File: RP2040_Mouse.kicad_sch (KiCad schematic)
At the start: 35 parts, among them J1 DB9_Male, J2 Barrel_Jack_Switch, J3 USB_A, Q1 Q_NPN_BEC, SW1 SW_DPDT_x2, U1 LSF0108PWR, U2 RP2040, U3 AT25SF081B-SSHD-T, U4 AMS1117-3.3, Y1 12MHZ

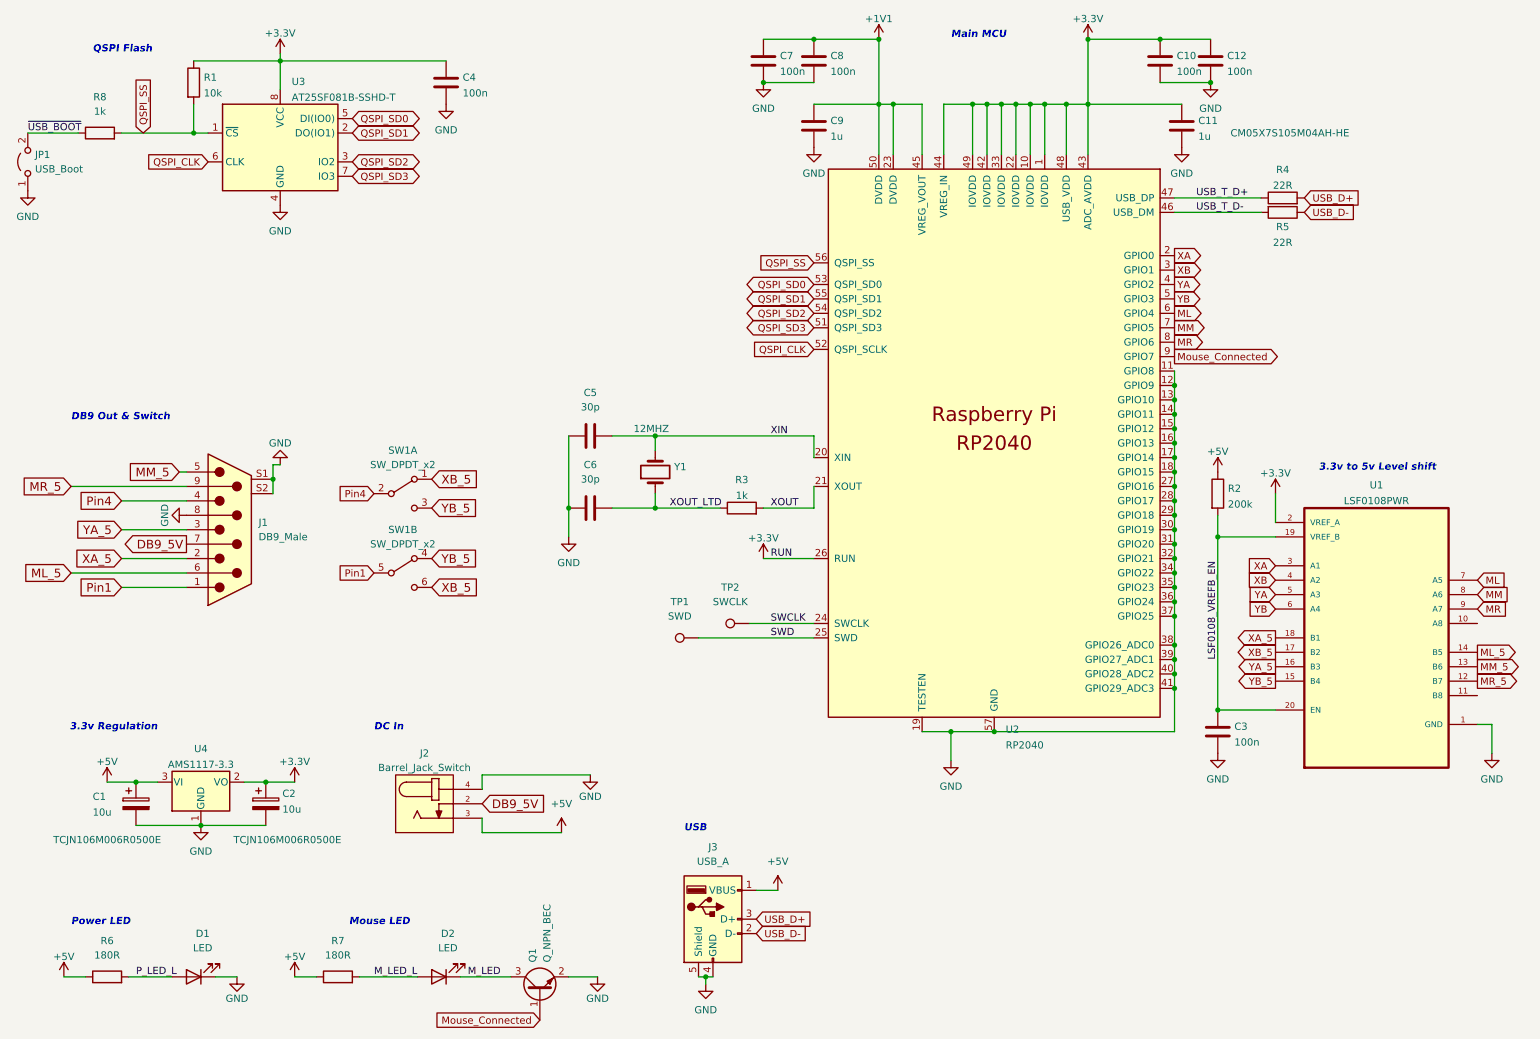
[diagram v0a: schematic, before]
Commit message: Added pullup resistors on mouse buttons, added breakout points for user software updates
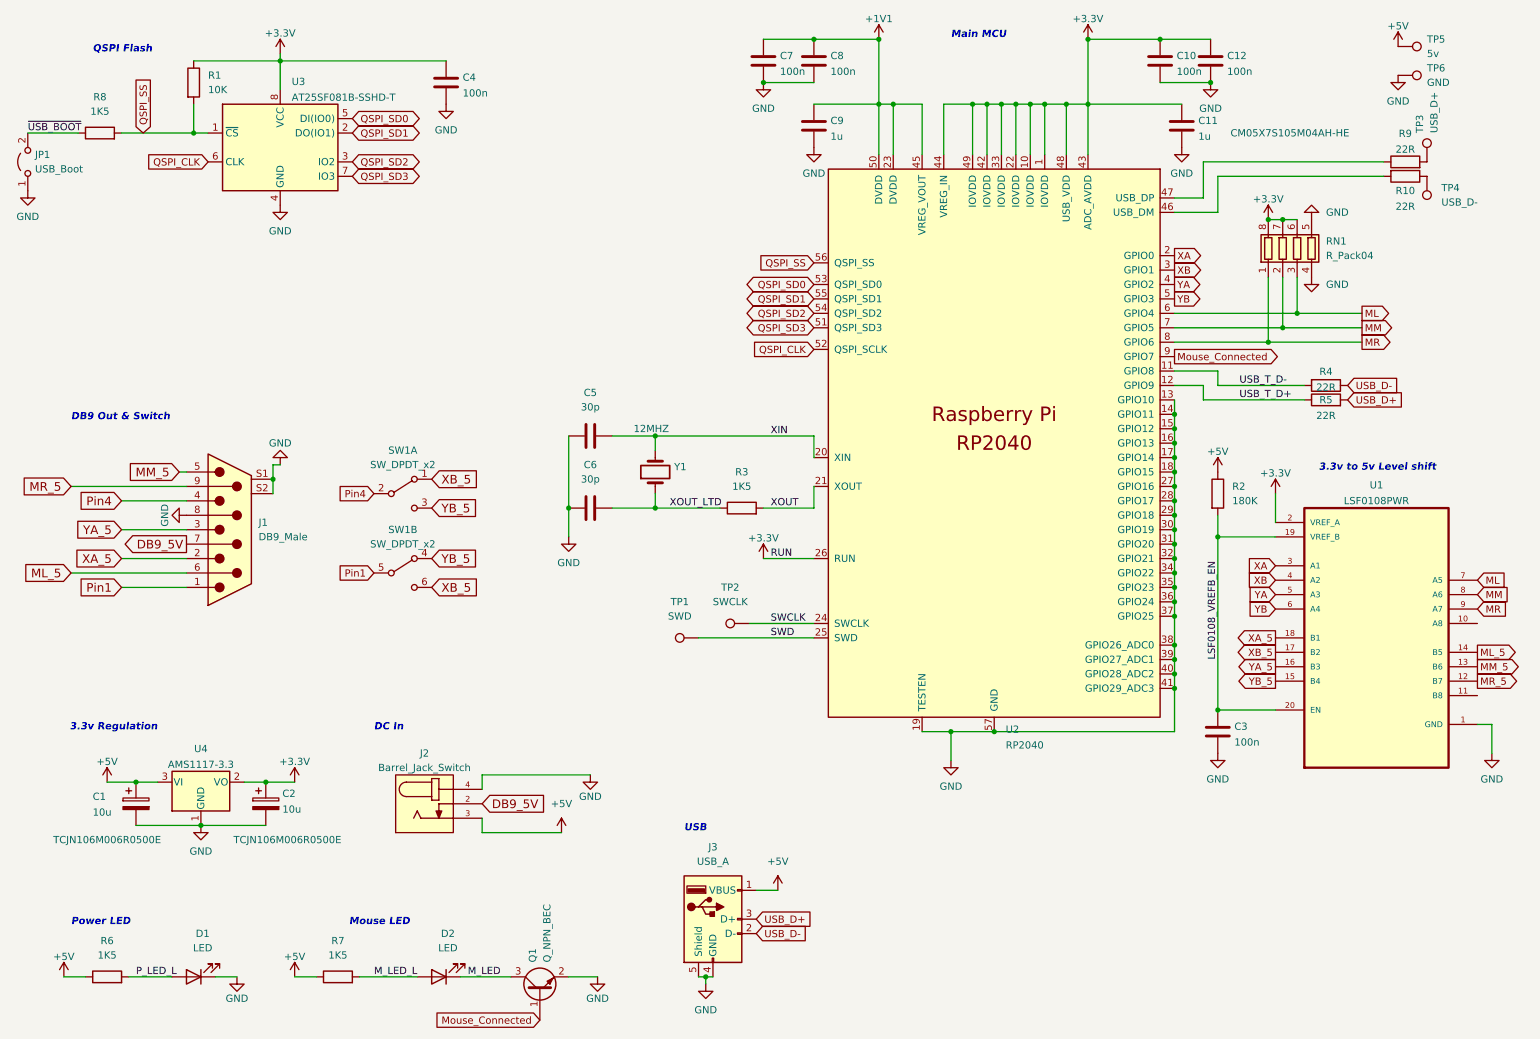
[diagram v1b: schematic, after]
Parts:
- added R10, R9: 22R, Resistor_SMD:R_0402_1005Metric, symbol Device:R
- added RN1: R_Pack04, symbol Device:R_Pack04
- added TP3: USB_D+, TestPoint:TestPoint_Pad_D1.0mm, symbol Connector:TestPoint
- added TP4: USB_D-, TestPoint:TestPoint_Pad_D1.0mm, symbol Connector:TestPoint
- added TP5: 5v, TestPoint:TestPoint_Pad_D1.0mm, symbol Connector:TestPoint
- added TP6: GND, TestPoint:TestPoint_Pad_D1.0mm, symbol Connector:TestPoint
- R1: value 10k -> 10K
- R2: value 200k -> 180K
- R3, R8: value 1k -> 1K5
- R6, R7: value 180R -> 1K5
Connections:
- net +3V3: now also RN1.6 (R3.2), RN1.7 (R2.2), RN1.8 (R1.2)
- net +5V: now also TP5.1
- net GND: now also RN1.4 (R4.1), RN1.5 (R4.2), TP6.1; no longer U2.11 (GPIO8), U2.12 (GPIO9)
- net ML: now also RN1.3 (R3.1)
- net MM: now also RN1.2 (R2.1)
- net MR: now also RN1.1 (R1.1)
- net USB_T_D+: now also U2.12 (GPIO9); no longer U2.47 (USB_DP)
- net USB_T_D-: now also U2.11 (GPIO8); no longer U2.46 (USB_DM)
- new net: R10.1, TP4.1
- new net: R10.2, U2.46 (USB_DM)
- new net: R9.1, U2.47 (USB_DP)
- new net: R9.2, TP3.1
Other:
- moved on the sheet: R4, R5

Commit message: New board not using default USB pins
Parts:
- RN1: footprint (none) -> Resistor_SMD:R_Array_Concave_4x0402
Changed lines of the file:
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@@
       (effects (font (size 1.27 1.27)) (justify left))
     )
-    (property "Footprint" "" (id 2) (at 250.825 57.15 90)
+    (property "Footprint" "Resistor_SMD:R_Array_Concave_4x0402" (id 2) (at 250.825 57.15 90)
       (effects (font (size 1.27 1.27)) hide)
     )

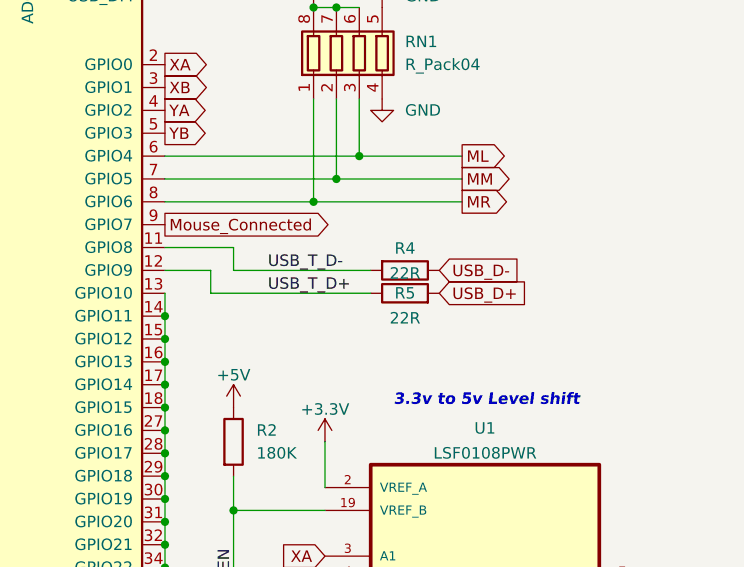
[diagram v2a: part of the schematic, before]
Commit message: Rev 4, swap the USB pins around to match the requirements of Tinyusb. Add PDF scematic Update 3d renders
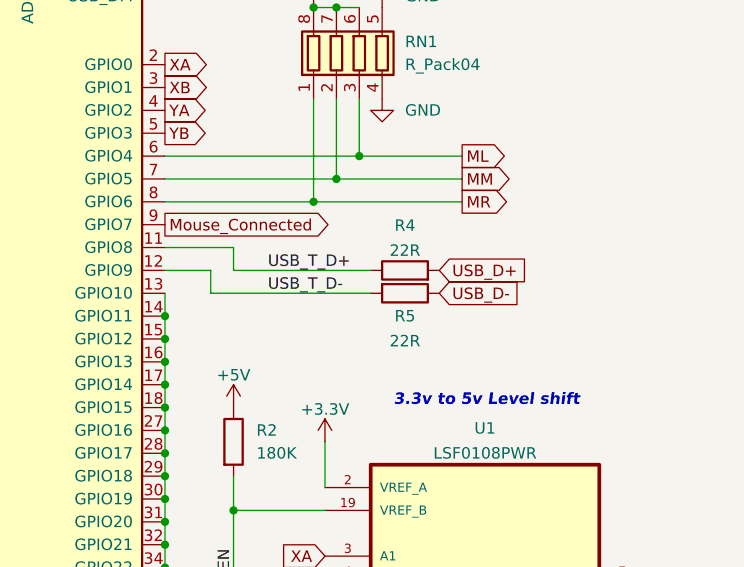
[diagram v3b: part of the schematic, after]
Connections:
- net USB_T_D+: now also U2.11 (GPIO8); no longer U2.12 (GPIO9)
- net USB_T_D-: now also U2.12 (GPIO9); no longer U2.11 (GPIO8)
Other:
- moved on the sheet: R4, R5
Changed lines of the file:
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@@
   (title_block
     (title "RP2040 USB to Quadrature Mouse Adaptor")
-    (date "2023-01-08")
-    (rev "3")
+    (date "2023-01-14")
+    (rev "4")
     (company "Darrens Lab")
   )
@@
     (effects (font (size 1.27 1.27)) (justify left bottom))
   )
-  (label "USB_T_D-" (at 233.68 81.28 0)
+  (label "USB_T_D-" (at 233.68 83.82 0)
     (effects (font (size 1.27 1.27)) (justify left bottom))
   )
@@
     (effects (font (size 1.27 1.27)) (justify left bottom))
   )
-  (label "USB_T_D+" (at 233.68 83.82 0)
+  (label "USB_T_D+" (at 233.68 81.28 0)
     (effects (font (size 1.27 1.27)) (justify left bottom))
   )
@@
     )
   )
-  (global_label "USB_D-" (shape input) (at 252.73 81.28 0) (fields_autoplaced)
-    (effects (font (size 1.27 1.27)) (justify left))
-    (property "Intersheet References" "${INTERSHEET_REFS}" (id 0) (at 262.7631 81.2006 0)
+  (global_label "USB_D-" (shape input) (at 252.73 83.82 0) (fields_autoplaced)
+    (effects (font (size 1.27 1.27)) (justify left))
+    (property "Intersheet References" "${INTERSHEET_REFS}" (id 0) (at 262.7631 83.7406 0)
       (effects (font (size 1.27 1.27)) (justify left) hide)
     )
@@
     )
   )
-  (global_label "USB_D+" (shape input) (at 252.73 83.82 0) (fields_autoplaced)
-    (effects (font (size 1.27 1.27)) (justify left))
-    (property "Intersheet References" "${INTERSHEET_REFS}" (id 0) (at 262.7631 83.7406 0)
+  (global_label "USB_D+" (shape input) (at 252.73 81.28 0) (fields_autoplaced)
+    (effects (font (size 1.27 1.27)) (justify left))
+    (property "Intersheet References" "${INTERSHEET_REFS}" (id 0) (at 262.7631 81.2006 0)
       (effects (font (size 1.27 1.27)) (justify left) hide)
     )
@@
     (pin "1")
   )
-  (symbol (lib_id "Device:R") (at 248.92 81.28 270) (unit 1)
+  (symbol (lib_id "Device:R") (at 248.92 83.82 270) (unit 1)
     (in_bom yes) (on_board yes)
-    (property "Reference" "R5" (id 0) (at 248.92 83.82 90))
-    (property "Value" "22R" (id 1) (at 248.92 86.5951 90))
-    (property "Footprint" "Resistor_SMD:R_0402_1005Metric" (id 2) (at 248.92 79.502 90)
-      (effects (font (size 1.27 1.27)) hide)
-    )
-    (property "Datasheet" "~" (id 3) (at 248.92 81.28 0)
+    (property "Reference" "R5" (id 0) (at 248.92 86.36 90))
+    (property "Value" "22R" (id 1) (at 248.92 89.1351 90))
+    (property "Footprint" "Resistor_SMD:R_0402_1005Metric" (id 2) (at 248.92 82.042 90)
+      (effects (font (size 1.27 1.27)) hide)
+    )
+    (property "Datasheet" "~" (id 3) (at 248.92 83.82 0)
       (effects (font (size 1.27 1.27)) hide)
     )
@@
     (pin "2")
   )
-  (symbol (lib_id "Device:R") (at 248.92 83.82 90) (unit 1)
-    (in_bom yes) (on_board yes) (fields_autoplaced)
-    (property "Reference" "R4" (id 0) (at 248.92 78.8375 90))
-    (property "Value" "22R" (id 1) (at 248.92 81.6126 90))
-    (property "Footprint" "Resistor_SMD:R_0402_1005Metric" (id 2) (at 248.92 85.598 90)
-      (effects (font (size 1.27 1.27)) hide)
-    )
-    (property "Datasheet" "~" (id 3) (at 248.92 83.82 0)
-      (effects (font (size 1.27 1.27)) hide)
-    )
+  (symbol (lib_id "Device:R") (at 248.92 81.28 90) (unit 1)
+    (in_bom yes) (on_board yes)
+    (property "Reference" "R4" (id 0) (at 248.92 76.2975 90))
+    (property "Value" "22R" (id 1) (at 248.92 79.0726 90))
+    (property "Footprint" "Resistor_SMD:R_0402_1005Metric" (id 2) (at 248.92 83.058 90)
+      (effects (font (size 1.27 1.27)) hide)
+    )
+    (property "Datasheet" "~" (id 3) (at 248.92 81.28 0)
+      (effects (font (size 1.27 1.27)) hide)
+    )

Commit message: Fix footprint issue from 2nd PCB run, pannelize for prod, new pics, new label
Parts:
- Q1: footprint Package_TO_SOT_SMD:SOT-323_SC-70 -> Package_TO_SOT_SMD:SOT-23-3
- U2: footprint Package_DFN_QFN:QFN-56-1EP_8x8mm_P0.5mm_EP4.3x4.3mm_ThermalVias -> Library:RP2040-QFN-56
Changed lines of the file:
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@@
   (title_block
     (title "RP2040 USB to Quadrature Mouse Adaptor")
-    (date "2023-01-14")
-    (rev "4")
+    (date "2023-01-21")
+    (rev "5")
     (company "Darrens Lab")
   )
@@
       (effects (font (size 1.27 1.27)) (justify left))
     )
-    (property "Footprint" "Package_TO_SOT_SMD:SOT-323_SC-70" (id 2) (at 107.95 182.88 0)
+    (property "Footprint" "Package_TO_SOT_SMD:SOT-23-3" (id 2) (at 107.95 182.88 0)
       (effects (font (size 1.27 1.27)) hide)
     )
@@
       (effects (font (size 1.27 1.27)) (justify left))
     )
-    (property "Footprint" "Package_DFN_QFN:QFN-56-1EP_8x8mm_P0.5mm_EP4.3x4.3mm_ThermalVias" (id 2) (at 171.45 91.44 0)
+    (property "Footprint" "Library:RP2040-QFN-56" (id 2) (at 171.45 91.44 0)
       (effects (font (size 1.27 1.27)) hide)
     )
@@
     )
     (path "/bb162b96-fbc5-4aa7-9f23-bc3be2dff577"
-      (reference "Q1") (unit 1) (value "Q_NPN_BEC") (footprint "Package_TO_SOT_SMD:SOT-323_SC-70")
+      (reference "Q1") (unit 1) (value "Q_NPN_BEC") (footprint "Package_TO_SOT_SMD:SOT-23-3")
     )
     (path "/053edd54-4904-42bd-8bde-773af7b0640e"
@@
     )
     (path "/f6832cc7-2a01-498f-b0bd-c34fbd7551b8"
-      (reference "U2") (unit 1) (value "RP2040") (footprint "Package_DFN_QFN:QFN-56-1EP_8x8mm_P0.5mm_EP4.3x4.3mm_ThermalVias")
+      (reference "U2") (unit 1) (value "RP2040") (footprint "Library:RP2040-QFN-56")
     )
     (path "/15cfbf4f-b005-4451-a70b-02ee25c9d0a5"

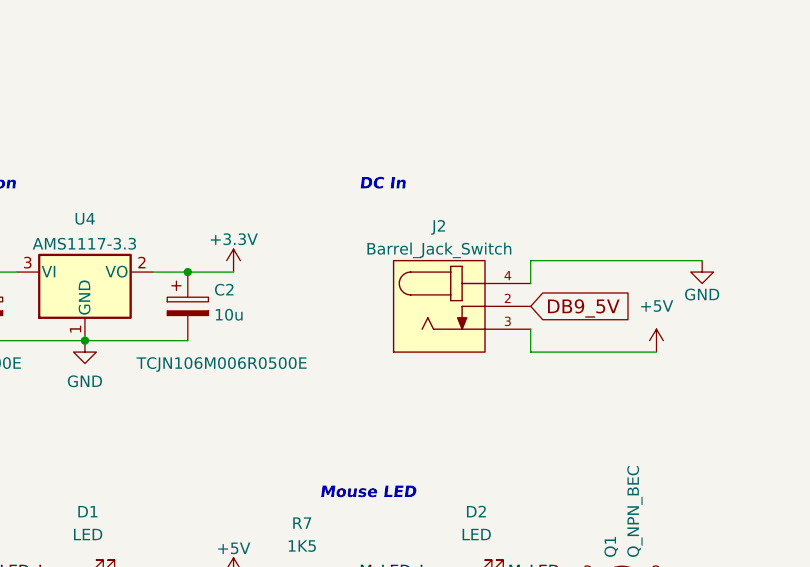
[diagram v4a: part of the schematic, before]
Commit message: Upgrade to KiCAD 6.99 (Nightly)
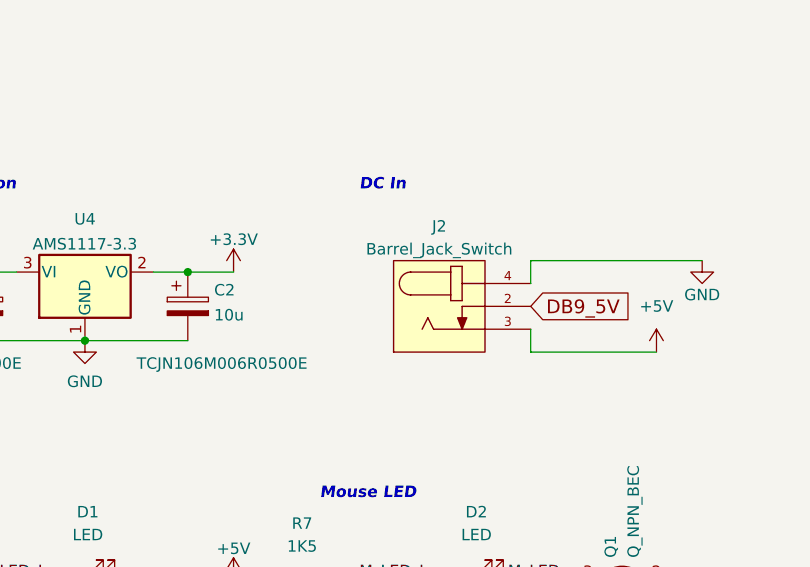
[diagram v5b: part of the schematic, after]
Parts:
- J1: footprint SmallyMouse QFN64-backups:ASSMANN_A-DF_09_A_KG-T2S -> My Library:ASSMANN_A-DF_09_A_KG-T2S
